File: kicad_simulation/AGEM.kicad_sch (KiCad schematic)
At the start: 49 parts, among them J1 Conn_01x03_Pin, J2 Conn_01x03_Pin, J3 Conn_01x03_Pin, J4 Conn_01x02_Pin, J5 Conn_01x02_Pin, J6 Conn_01x03_Pin, Q1 2N5457, SW1 SW_SPST, U1 TL072, U2 TL072

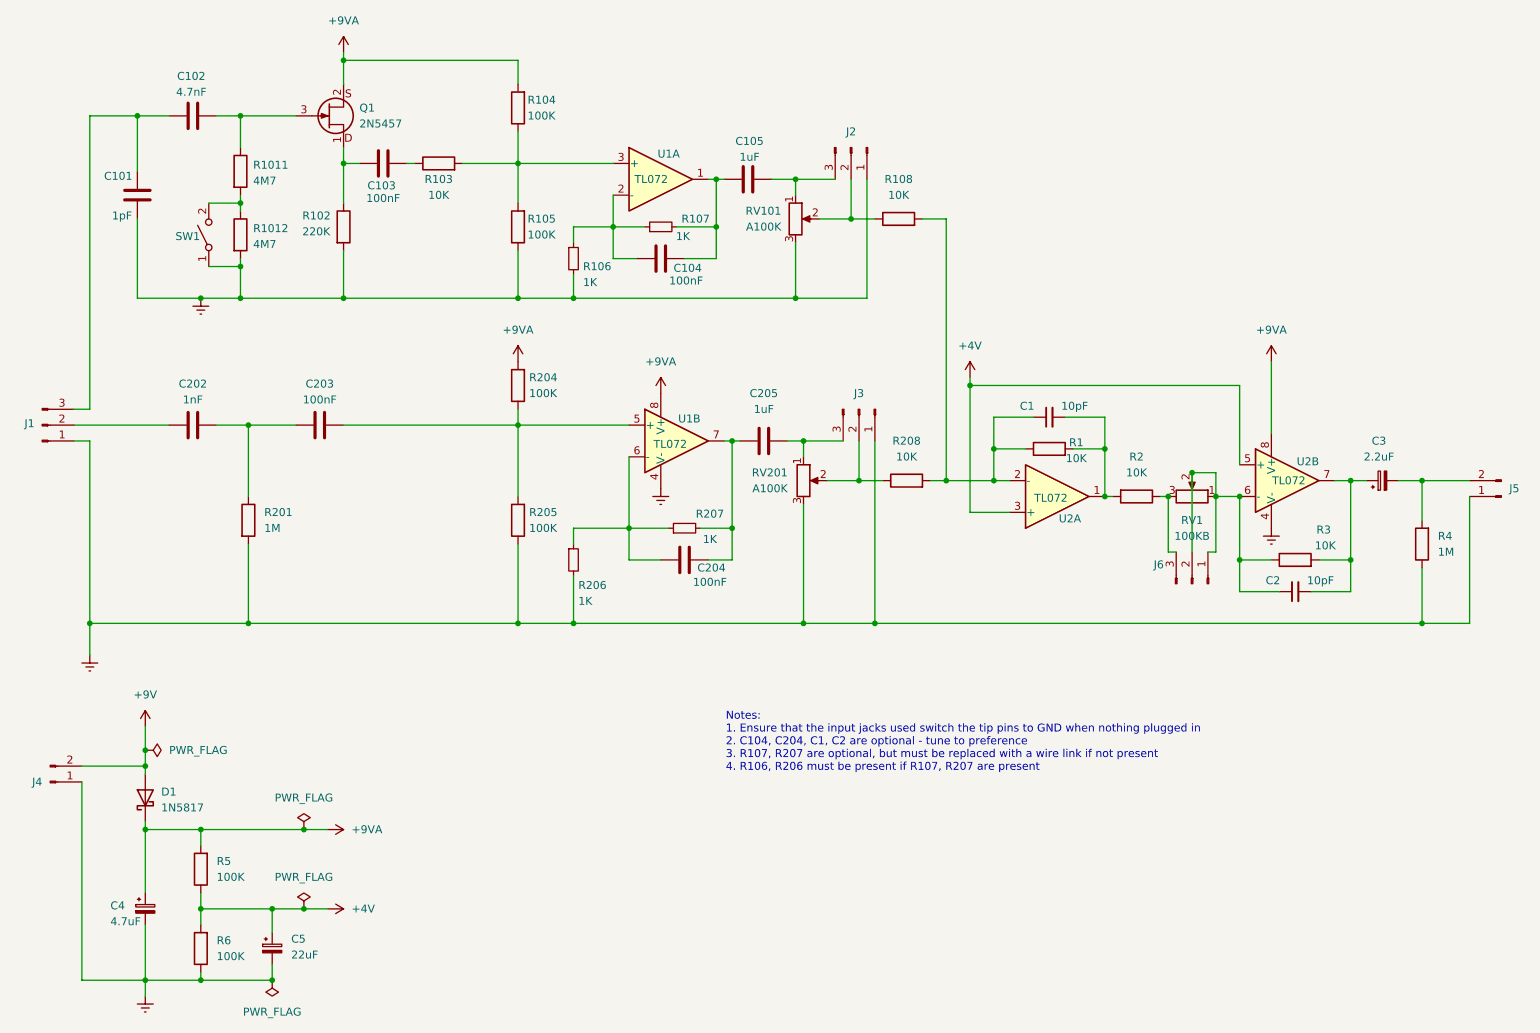
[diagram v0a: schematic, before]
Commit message: Added simulation and updated schematic to V1.2 based on simulation
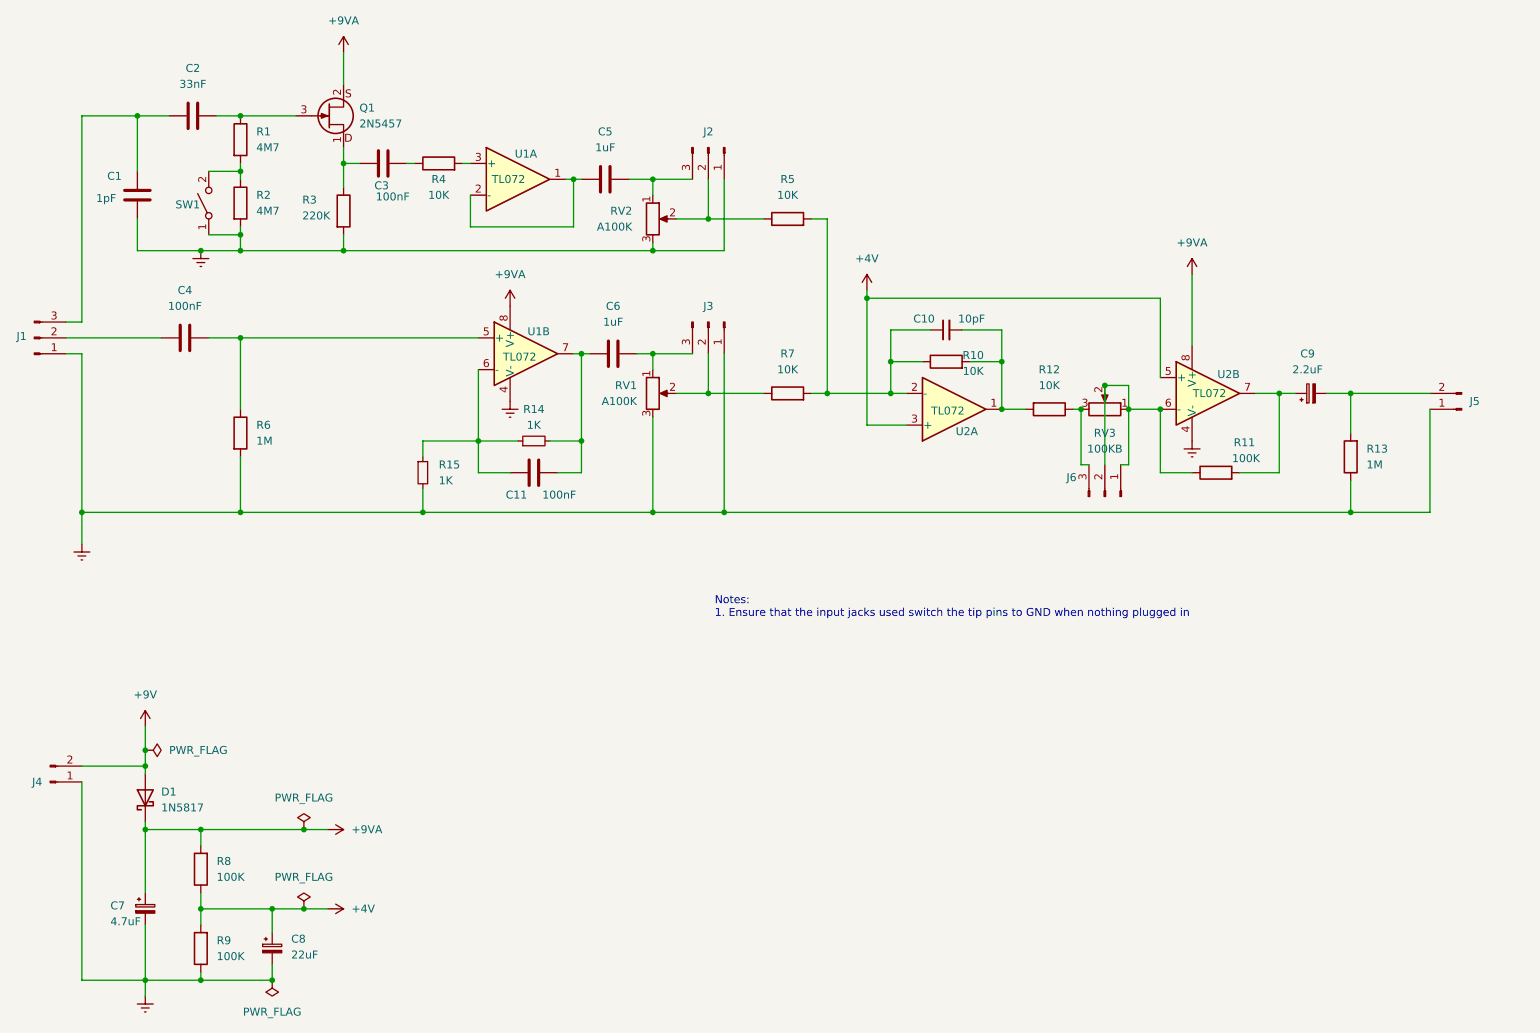
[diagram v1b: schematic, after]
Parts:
- removed C1, C2: 10pF, Capacitor_THT:C_Disc_D4.3mm_W1.9mm_P5.00mm, symbol Device:C_Small
- removed C104, C203: 100nF, Capacitor_THT:C_Rect_L7.2mm_W2.5mm_P5.00mm_FKS2_FKP2_MKS2_MKP2, symbol Device:C
- removed R104, R105, R204, R205: 100K, Resistor_THT:R_Axial_DIN0207_L6.3mm_D2.5mm_P10.16mm_Horizontal, symbol Device:R
- removed R106, R107: 1K, Resistor_THT:R_Axial_DIN0207_L6.3mm_D2.5mm_P10.16mm_Horizontal, symbol Device:R_Small
- added C10: 10pF, Capacitor_THT:C_Disc_D4.3mm_W1.9mm_P5.00mm, symbol Device:C_Small
- C2: renamed from C102; value 4.7nF -> 33nF
- C4: renamed from C202; value 1nF -> 100nF
- R11: renamed from R3; value 10K -> 100K
- renumbered C101 to C1, C204 to C11, C103 to C3, C105 to C5, C205 to C6, C4 to C7, C5 to C8, C3 to C9, R1011 to R1, R1 to R10, R2 to R12, R4 to R13, R207 to R14, R206 to R15, R1012 to R2, R102 to R3, R103 to R4, R108 to R5, R201 to R6, R208 to R7, R5 to R8, R6 to R9, RV201 to RV1, RV101 to RV2, RV1 to RV3
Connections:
- net at R10.1, R5.2, R7.2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: now also C10.1
- net at R10.2, R12.2, U2.1: now also C10.2
- net at C4.2, R6.1: now also U1.5 (+)
- net at U1.2 (-): now also C5.1, U1.1
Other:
- note added: "Notes: 1. Ensure that the input jacks used switch the tip pins to GND when nothing plugged in"
- note removed: "Notes: 1. Ensure that the input jacks used switch the tip pins to GND when nothing plugged in 2. C104, C204, C1, C2 are optional - tune to preference 3. R107, R207 are optional, but must be replaced with a wire link if not present 4. R106, R206 must be present if R107, R207 are present"
- moved on the sheet: C11, C4, C5, C6, C9, J1, J2, J3, J5, J6, R1, R10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
